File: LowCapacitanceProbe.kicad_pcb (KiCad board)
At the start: 2 copper layers, 35.6 x 58.5 mm, 41 parts, among them J1 u.Fl, J2 SMA, J4 7792, Q1 BF998, U2 SPX3819M5-L-5-0

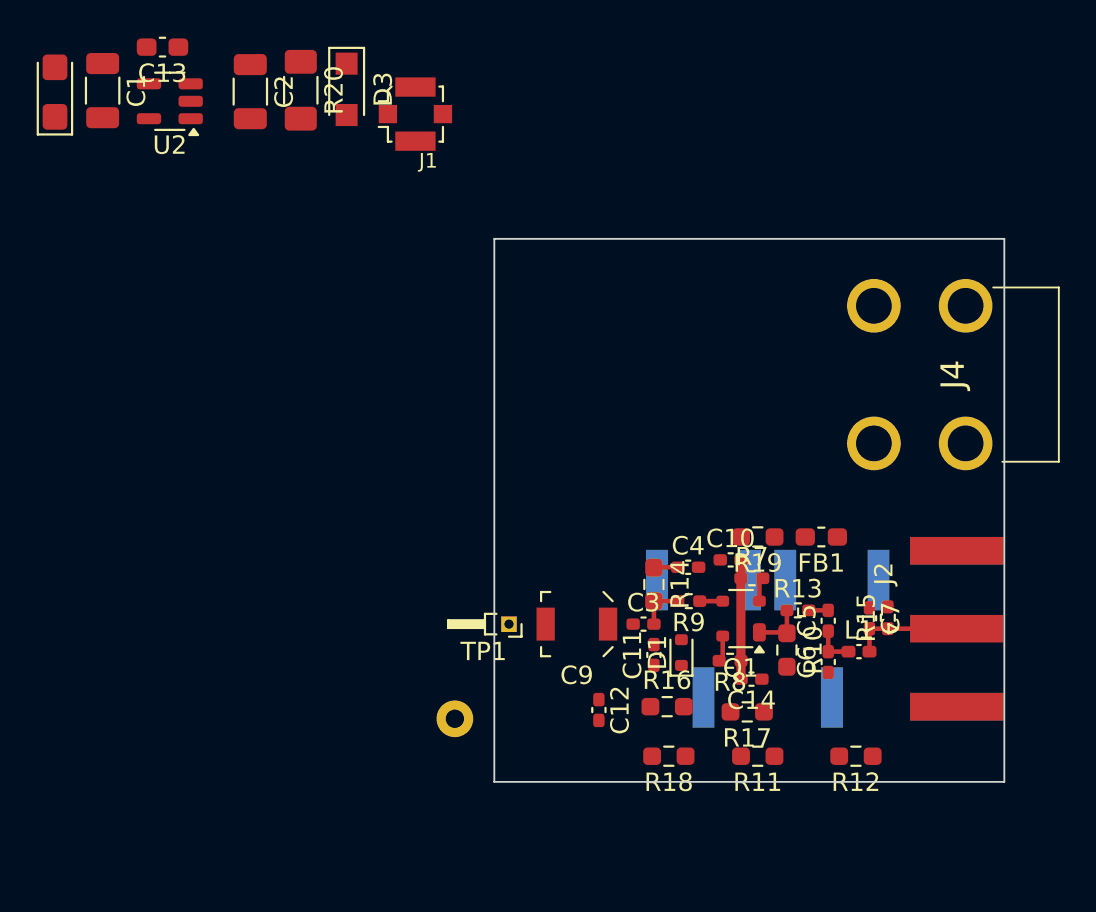
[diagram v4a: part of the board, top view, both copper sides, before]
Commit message: Continued routing, modifications for better usability.
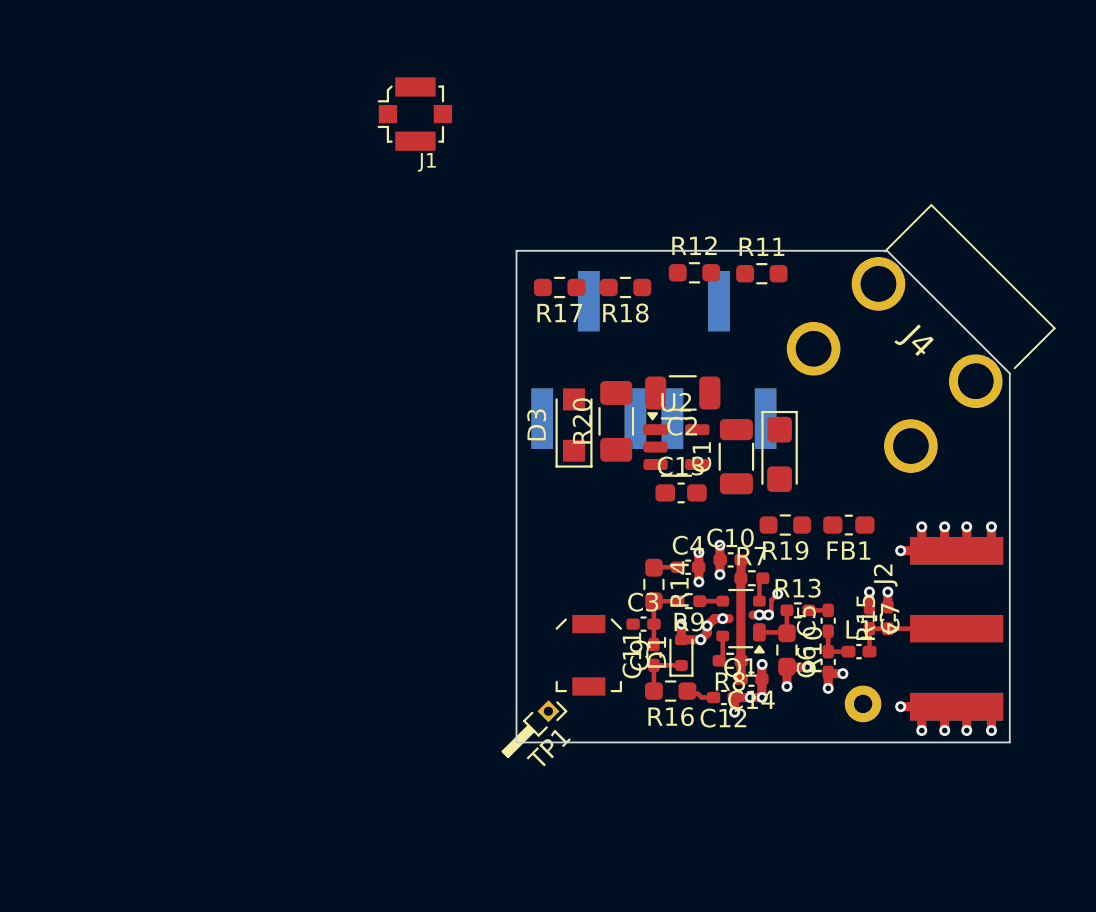
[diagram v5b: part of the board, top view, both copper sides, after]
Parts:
- moved C8 44.2 mm to (125.3, 60.8), turned to -90 degrees
- moved C1 39.9 mm to (123.0, 60.9), turned to 90 degrees
- moved C13 37.3 mm to (120.0, 62.9), turned to 0 degrees
- moved U2 33.4 mm to (119.7, 60.4), turned to 0 degrees
- moved C2 28.7 mm to (120.1, 57.4), turned to 180 degrees
- moved R12 27.8 mm to (120.7, 50.9), turned to 0 degrees
- moved R11 26.3 mm to (124.4, 50.9), turned to 0 degrees
- moved R18 25.7 mm to (117.0, 51.6)
- moved R17 25.3 mm to (113.4, 51.6)
- moved R20 24.9 mm to (116.4, 59.0), turned to 90 degrees
- moved TP3 22.3 mm to (129.9, 74.3)
- moved D3 22.1 mm to (114.1, 59.1), turned to 90 degrees
- moved RV2 16.4 mm to (115.0, 55.6), turned to -90 degrees
- moved RV3 16.4 mm to (122.0, 55.6), turned to -90 degrees
- moved C12 6.85 mm to (122.3, 74.0), turned to 180 degrees
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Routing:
- net GND: track 0.00 -> 45.8 mm, vias 54 -> 85
- net Net-(D1-K): track 0.00 -> 2.90 mm
- net /GAIN_TUNE: track 0.00 -> 1.58 mm
- net /IN_2: track 2.56 -> 3.67 mm
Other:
- board size 35.6 x 58.5 mm -> 35.9 x 57.9 mm

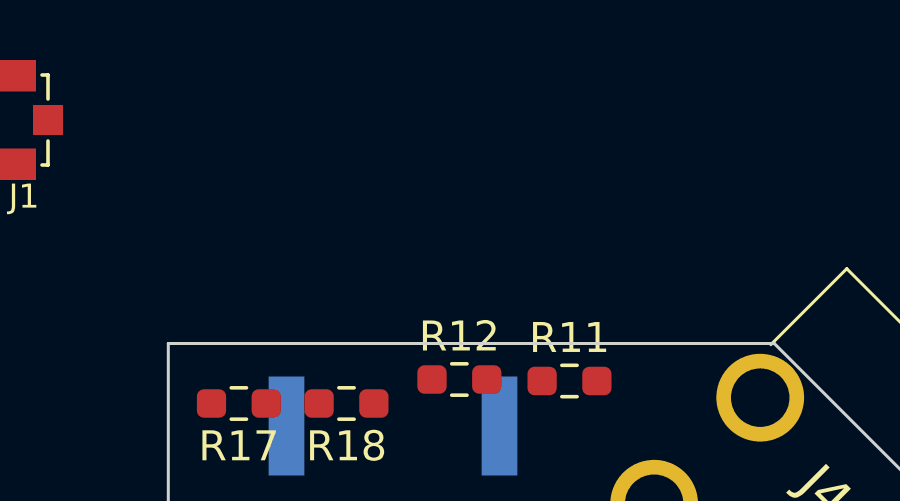
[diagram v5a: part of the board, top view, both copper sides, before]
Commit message: Synchronisation of computers, some tiny changes to simulation.
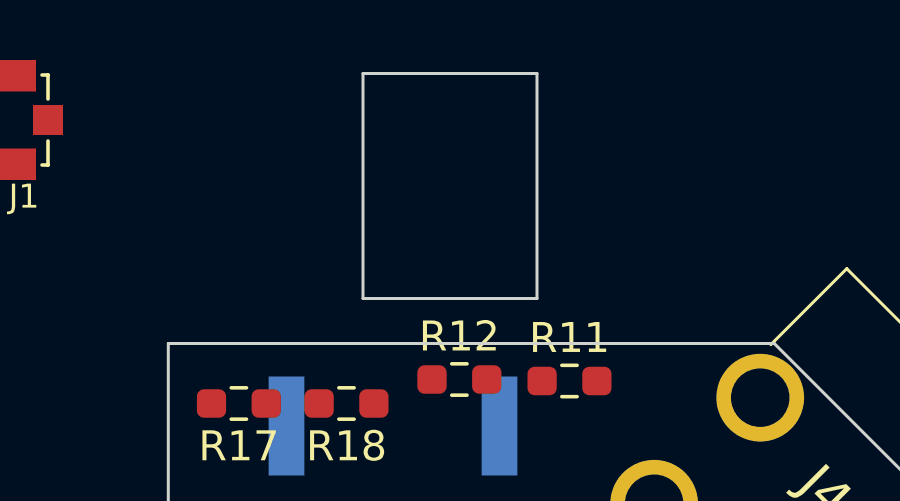
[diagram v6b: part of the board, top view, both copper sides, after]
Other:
- board size 35.9 x 57.9 mm -> 35.9 x 66.8 mm
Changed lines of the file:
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@@
+		(layer "Edge.Cuts")
+	)
+	(gr_rect
+		(start 117.5 48.15)
+		(end 123.3 40.65)
+		(stroke
+			(width 0.1)
+			(type solid)
+		)
+		(fill no)
 		(layer "Edge.Cuts")
 	)

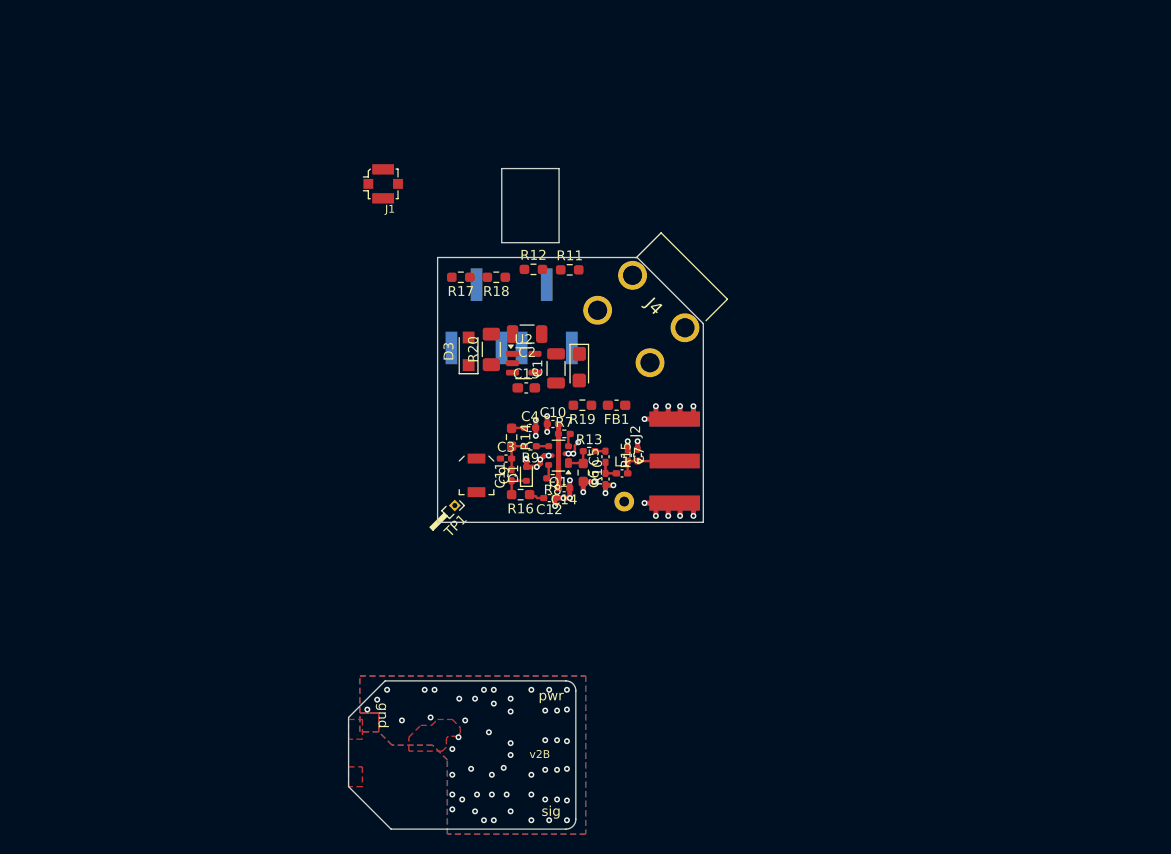
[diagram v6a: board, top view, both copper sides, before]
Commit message: Continued routing, replaced power connector.
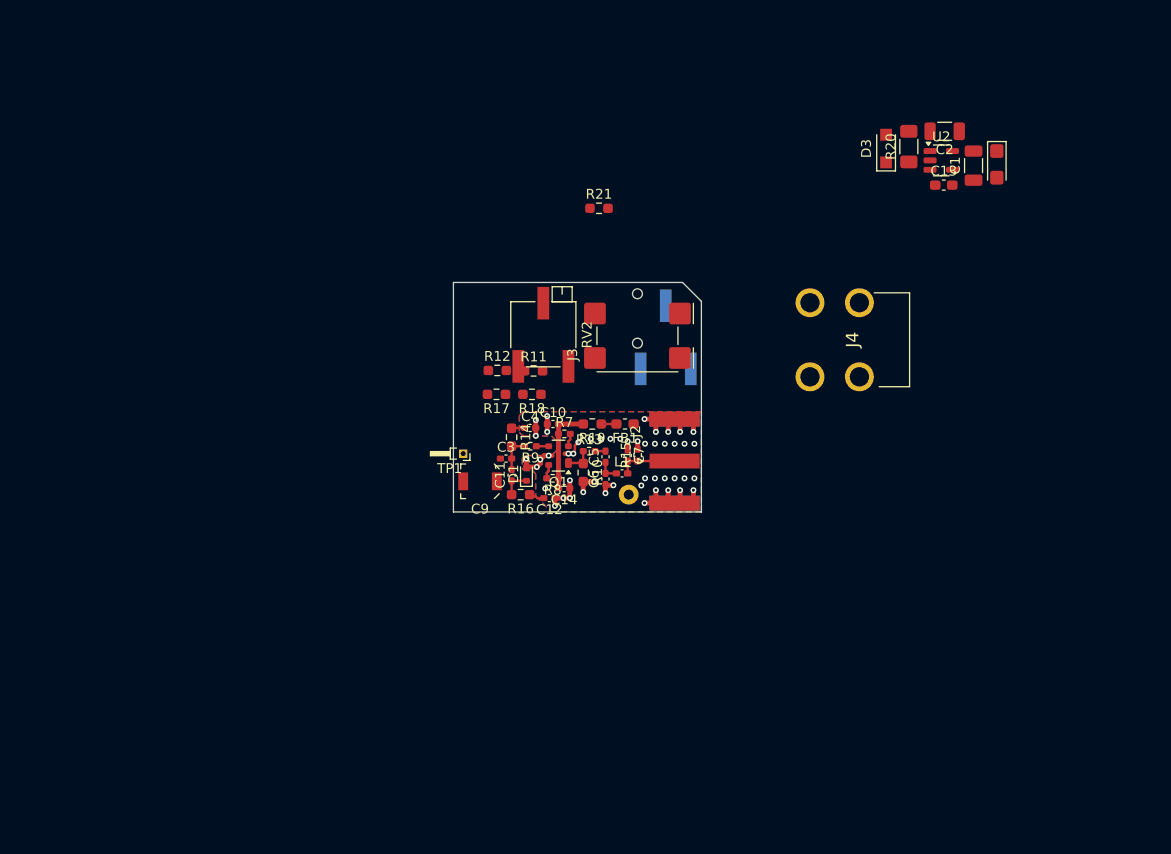
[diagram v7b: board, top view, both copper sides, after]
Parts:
- removed J1: u.Fl, Connector_Coaxial:U.FL_Molex_MCRF_73412-0110_Vertical
- added J3: Barrel_Jack_Switch, Connector_BarrelJack:BarrelJack_Wuerth_694103107102_1.35x3.9mm, F.Cu at (131.2, 56.5)
- added R21: 10k, Resistor_SMD:R_0603_1608Metric_Pad0.98x0.95mm_HandSolder, F.Cu at (127.3, 44.7)
- RV2: moved to F.Cu
- moved C13 47.0 mm to (162.2, 42.3)
- moved D3 47.0 mm to (156.4, 38.6)
- moved C1 47.0 mm to (165.2, 40.4)
- moved C2 47.0 mm to (162.3, 36.9)
- moved C8 47.0 mm to (167.6, 40.2)
- moved R20 47.0 mm to (158.7, 38.4)
- moved U2 47.0 mm to (162.0, 39.8)
- moved J4 21.5 mm to (148.7, 54.2), turned to -90 degrees
- moved R17 12.4 mm to (117.0, 63.5)
- moved R18 12.4 mm to (120.6, 63.5)
- moved RV3 12.2 mm to (134.1, 57.7)
- moved R11 10.9 mm to (120.7, 61.1)
- moved R12 10.9 mm to (117.1, 61.1)
- moved RV2 7.01 mm to (121.7, 57.5)
- moved TP1 5.32 mm to (113.6, 69.5), turned to 180 degrees
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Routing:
- net /POWER: track 6.51 -> 9.01 mm
- net Net-(FB1-Pad2): track 0.00 -> 1.52 mm
- net GND: vias 85 -> 49
- removed copper zone on F.Cu, net (none)
- removed copper zone on F.Cu, net +5V
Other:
- board size 35.9 x 66.8 mm -> 25.1 x 23.2 mm
- board text removed: "10x, 1.3 GHz"
- board text removed: "5-16V, 50 mA"
- board text removed: "FETProbe"
- board text removed: "Remove this sidewall"
- board text removed: "gnd"
- board text removed: "pwr"
- board text removed: "sig"
- board text removed: "v2B"

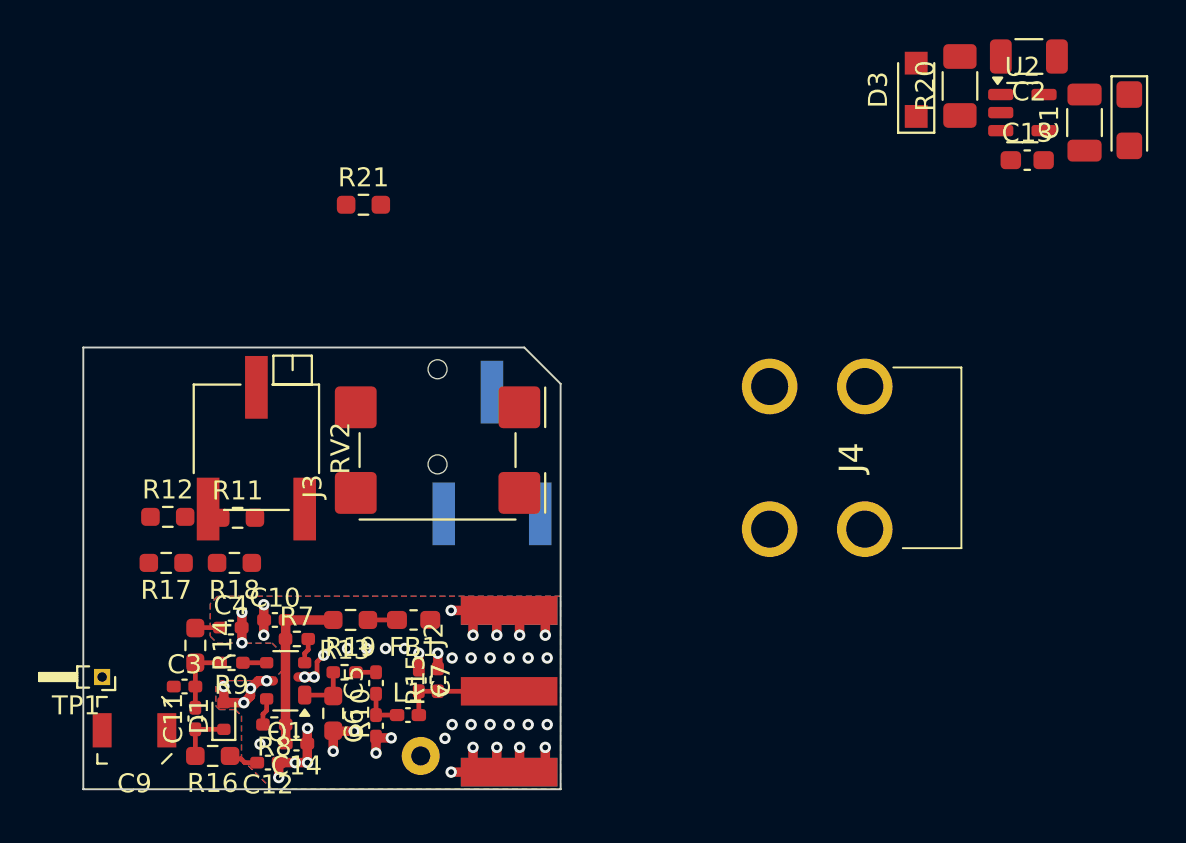
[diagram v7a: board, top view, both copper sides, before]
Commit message: Replaced trimmers, added 3D models, continued routing and placing.
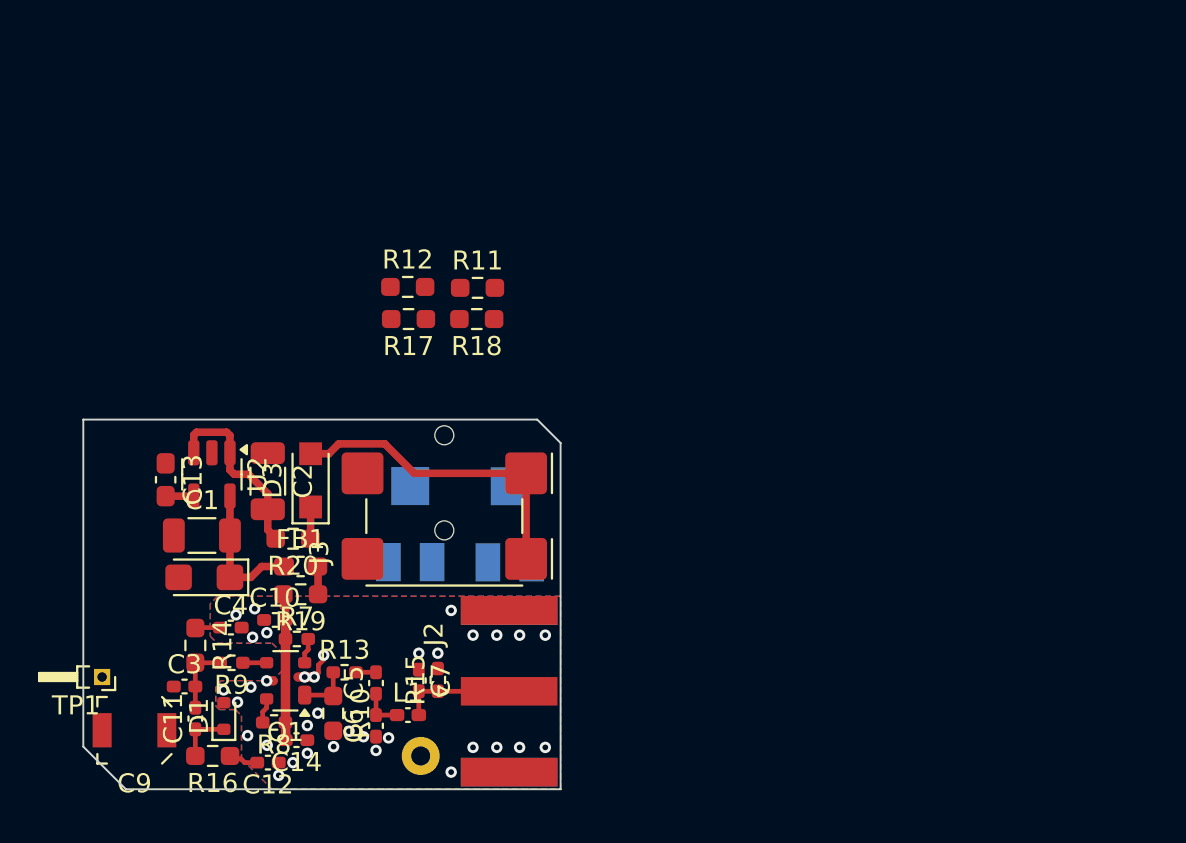
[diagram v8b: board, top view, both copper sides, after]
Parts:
- removed J4: 7792, 7792:7792
- removed R21: 10k, Resistor_SMD:R_0603_1608Metric_Pad0.98x0.95mm_HandSolder
- R20: value 10R -> 47R; footprint Resistor_SMD:R_1206_3216Metric_Pad1.30x1.75mm_HandSolder -> Resistor_SMD:R_0603_1608Metric_Pad0.98x0.95mm_HandSolder
- RV2: footprint Potentiometer_SMD:Potentiometer_Bourns_3269P_Horizontal -> Potentiometer_SMD:Potentiometer_Bourns_3214J_Horizontal; moved to B.Cu
- RV3: footprint Potentiometer_SMD:Potentiometer_Bourns_3269P_Horizontal -> Potentiometer_SMD:Potentiometer_Bourns_3214J_Horizontal
- moved C8 54.2 mm to (119.0, 64.3), turned to 180 degrees
- moved C1 51.2 mm to (118.8, 62.1), turned to 0 degrees
- moved C13 48.3 mm to (116.9, 59.1), turned to -90 degrees
- moved U2 46.7 mm to (119.4, 58.8), turned to -90 degrees
- moved C2 45.8 mm to (122.3, 59.2), turned to -90 degrees
- moved R20 42.4 mm to (123.6, 62.2), turned to 180 degrees
- moved D3 37.9 mm to (124.6, 59.2)
- moved R17 18.1 mm to (129.7, 50.7)
- moved R18 18.1 mm to (133.3, 50.7)
- moved R11 17.5 mm to (133.3, 49.0)
- moved R12 17.5 mm to (129.7, 49.0)
- moved RV2 9.02 mm to (129.8, 61.5)
- moved FB1 6.57 mm to (124.0, 63.7), turned to 0 degrees
- moved RV3 3.86 mm to (135.0, 61.5)
- moved J3 3.49 mm to (131.6, 59.9)
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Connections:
- J3 pad 3: Net-(J3-Pad3) -> unconnected-(J3-Pad3)
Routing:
- net GND: track 45.8 -> 12.8 mm, vias 49 -> 35
- net /PIN: track 0.00 -> 16.7 mm
- net /PIN_FILT: track 0.00 -> 9.83 mm
- net +5V: track 0.00 -> 7.35 mm
- net Net-(D3-K): track 0.00 -> 1.67 mm
- net /BYPASS: track 0.00 -> 1.48 mm
- net /POWER: track 9.01 -> 7.73 mm
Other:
- board size 25.1 x 23.2 mm -> 25.1 x 19.4 mm
